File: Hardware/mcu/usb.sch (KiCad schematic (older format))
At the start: 4 parts, among them U901 MINIUSB-B, U902 USBLC6-2

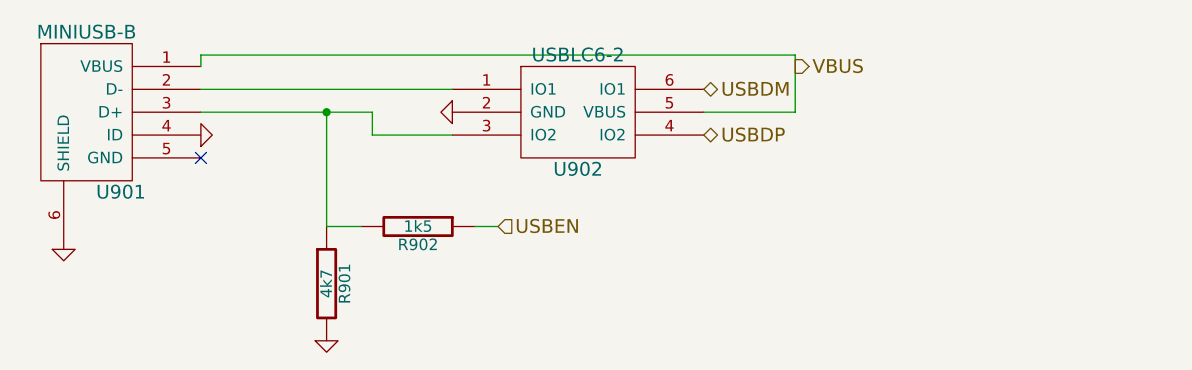
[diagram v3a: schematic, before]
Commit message: changes to mcu, new format and using a display adapter board
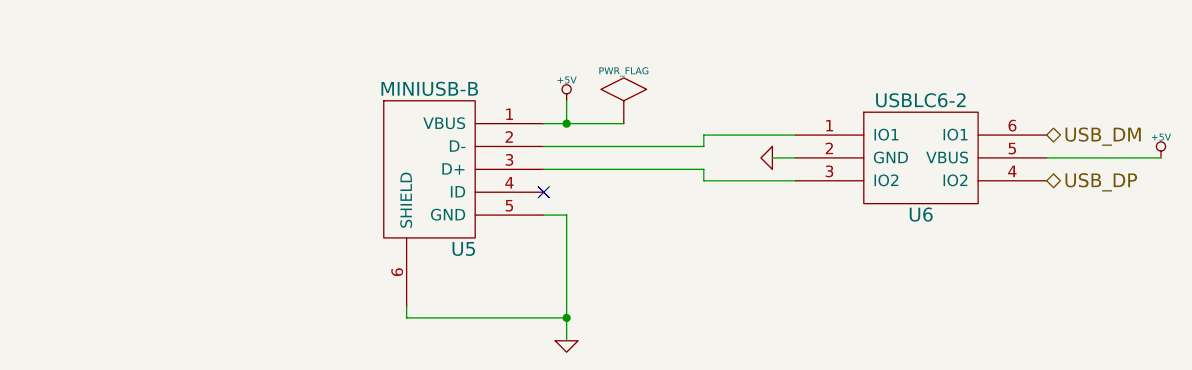
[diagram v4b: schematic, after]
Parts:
- removed R901: 4k7, symbol R
- removed R902: 1k5, symbol R
- removed U901: MINIUSB-B, symbol MINIUSB-B
- removed U902: USBLC6-2, symbol USBLC6-2
- added U5: MINIUSB-B, symbol MINIUSB-B
- added U6: USBLC6-2, symbol USBLC6-2
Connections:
- net GND: now also U5.5 (GND), U5.6 (SHIELD), U6.2 (GND)
- new net: U5.2 (D-), U6.1 (IO1)
- new net: U5.3 (D+), U6.3 (IO2)
- new net +5V: U5.1 (VBUS), U6.5 (VBUS)
- new net USB_DM: U6.6 (IO1)
- new net USB_DP: U6.4 (IO2)
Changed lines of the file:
@@
-EESchema Schematic File Version 2  date Di 17 Mai 2011 02:16:23 CEST
+EESchema Schematic File Version 2  date So 17 Jul 2011 02:24:17 CEST
 LIBS:power
 LIBS:device
@@
 LIBS:valves
 LIBS:nhesse
-LIBS:bordcomputer-cache
+LIBS:mcu-cache
 EELAYER 25  0
 EELAYER END
@@
 Sheet 7 9
 Title ""
-Date "17 may 2011"
+Date "16 jul 2011"
 Rev ""
 Comp ""
@@
 Comment4 ""
 $EndDescr
+Connection ~ 3500 1450
 Wire Wire Line
-	3100 1900 3200 1900
-Connection ~ 2450 1400
+	3750 1450 3400 1450
 Wire Wire Line
-	2450 1400 2450 1900
+	3400 1850 3500 1850
 Wire Wire Line
-	3000 1500 2650 1500
+	3500 1850 3500 2400
 Wire Wire Line
-	2650 1500 2650 1400
+	6100 1600 5600 1600
 Wire Wire Line
-	2650 1400 1900 1400
+	4500 1500 4100 1500
 Wire Wire Line
-	1900 1300 3000 1300
+	4100 1500 4100 1550
 Wire Wire Line
-	1900 1200 1900 1150
+	4100 1550 3400 1550
 Wire Wire Line
-	1900 1150 4500 1150
+	3500 1450 3500 1350
 Wire Wire Line
-	4500 1150 4500 1400
+	4500 1700 4100 1700
 Wire Wire Line
-	4500 1400 4100 1400
+	4100 1700 4100 1650
 Wire Wire Line
-	2450 1900 2600 1900
-Text HLabel 3200 1900 2    60   Input ~ 0
-USBEN
+	4100 1650 3400 1650
+Wire Wire Line
+	4400 1600 4500 1600
+Wire Wire Line
+	3500 2300 2800 2300
+Wire Wire Line
+	2800 2300 2800 2250
+Connection ~ 3500 2300
 $Comp
-L GND #PWR040
-U 1 1 4D743606
-P 2450 2400
-F 0 "#PWR040" H 2450 2400 30  0001 C CNN
-F 1 "GND" H 2450 2330 30  0001 C CNN
-	1    2450 2400
+L PWR_FLAG #FLG030
+U 1 1 4E17C6DB
+P 3750 1450
+F 0 "#FLG030" H 3750 1720 30  0001 C CNN
+F 1 "PWR_FLAG" H 3750 1680 30  0000 C CNN
+	1    3750 1450
+	1    0    0    -1
+$EndComp
+NoConn ~ 3400 1750
+$Comp
+L GND #PWR031
+U 1 1 4E1763AA
+P 3500 2400
+F 0 "#PWR031" H 3500 2400 30  0001 C CNN
+F 1 "GND" H 3500 2330 30  0001 C CNN
+	1    3500 2400
 	1    0    0    -1
 $EndComp
 $Comp
-L R R902
-U 1 1 4D7435FB
-P 2850 1900
-F 0 "R902" V 2930 1900 50  0000 C CNN
-F 1 "1k5" V 2850 1900 50  0000 C CNN
-	1    2850 1900
+L GND #PWR032
+U 1 1 4E1763A2
+P 4400 1600
+F 0 "#PWR032" H 4400 1600 30  0001 C CNN
+F 1 "GND" H 4400 1530 30  0001 C CNN
+	1    4400 1600
 	0    1    1    0
 $EndComp
 $Comp
-L R R901
-U 1 1 4D7435F8
-P 2450 2150
-F 0 "R901" V 2530 2150 50  0000 C CNN
-F 1 "4k7" V 2450 2150 50  0000 C CNN
-	1    2450 2150
+L +5V #PWR033
+U 1 1 4E17639B
+P 6100 1600
+F 0 "#PWR033" H 6100 1690 20  0001 C CNN
+F 1 "+5V" H 6100 1690 30  0000 C CNN
+	1    6100 1600
 	1    0    0    -1
 $EndComp
-Text HLabel 4500 1200 2    60   Output ~ 0
-VBUS
-Text HLabel 4100 1500 2    60   BiDi ~ 0
-USBDP
-Text HLabel 4100 1300 2    60   BiDi ~ 0
-USBDM
+Text HLabel 5600 1700 2    60   BiDi ~ 0
+USB_DP
+Text HLabel 5600 1500 2    60   BiDi ~ 0
+USB_DM
 $Comp
-L GND #PWR041
-U 1 1 4D74357C
-P 3000 1400
-F 0 "#PWR041" H 3000 1400 30  0001 C CNN
-F 1 "GND" H 3000 1330 30  0001 C CNN
-	1    3000 1400
-	0    1    1    0
-$EndComp
-$Comp
-L USBLC6-2 U902
-U 1 1 4D74356C
-P 3550 1400
-F 0 "U902" H 3550 1150 60  0000 C CNN
-F 1 "USBLC6-2" H 3550 1650 60  0000 C CNN
-	1    3550 1400
-	1    0    0    -1
-$EndComp
-NoConn ~ 1900 1600
-$Comp
-L GND #PWR042
-U 1 1 4D7434C4
-P 1900 1500
-F 0 "#PWR042" H 1900 1500 30  0001 C CNN
-F 1 "GND" H 1900 1430 30  0001 C CNN
-	1    1900 1500
-	0    -1   -1   0
-$EndComp
-$Comp
-L GND #PWR043
-U 1 1 4D7434C1
-P 1300 2000
-F 0 "#PWR043" H 1300 2000 30  0001 C CNN
-F 1 "GND" H 1300 1930 30  0001 C CNN
-	1    1300 2000
+L USBLC6-2 U6
+U 1 1 4E176372
+P 5050 1600
+F 0 "U6" H 5050 1350 60  0000 C CNN
+F 1 "USBLC6-2" H 5050 1850 60  0000 C CNN
+	1    5050 1600
 	1    0    0    -1
 $EndComp
 $Comp
-L MINIUSB-B U901
-U 1 1 4D7434BC
-P 1550 1550
-F 0 "U901" H 1550 1350 60  0000 C CNN
-F 1 "MINIUSB-B" H 1400 2050 60  0000 C CNN
-	1    1550 1550
+L +5V #PWR034
+U 1 1 4E176348
+P 3500 1350
+F 0 "#PWR034" H 3500 1440 20  0001 C CNN
+F 1 "+5V" H 3500 1440 30  0000 C CNN
+	1    3500 1350
 	1    0    0    -1
 $EndComp
+$Comp
+L MINIUSB-B U5
+U 1 1 4E176340
+P 3050 1800
+F 0 "U5" H 3050 1600 60  0000 C CNN
+F 1 "MINIUSB-B" H 2900 2300 60  0000 C CNN
+	1    3050 1800
+	1    0    0    -1
+$EndComp
